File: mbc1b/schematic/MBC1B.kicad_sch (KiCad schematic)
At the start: 25 parts, among them U1 ODRV, U10 ODRV, U2 ODRV, U3 ODRV, U4 ODRV, U5 ODRV, U6 ODRV, U7 ODRV, U8 ODRV, U9 ODRV

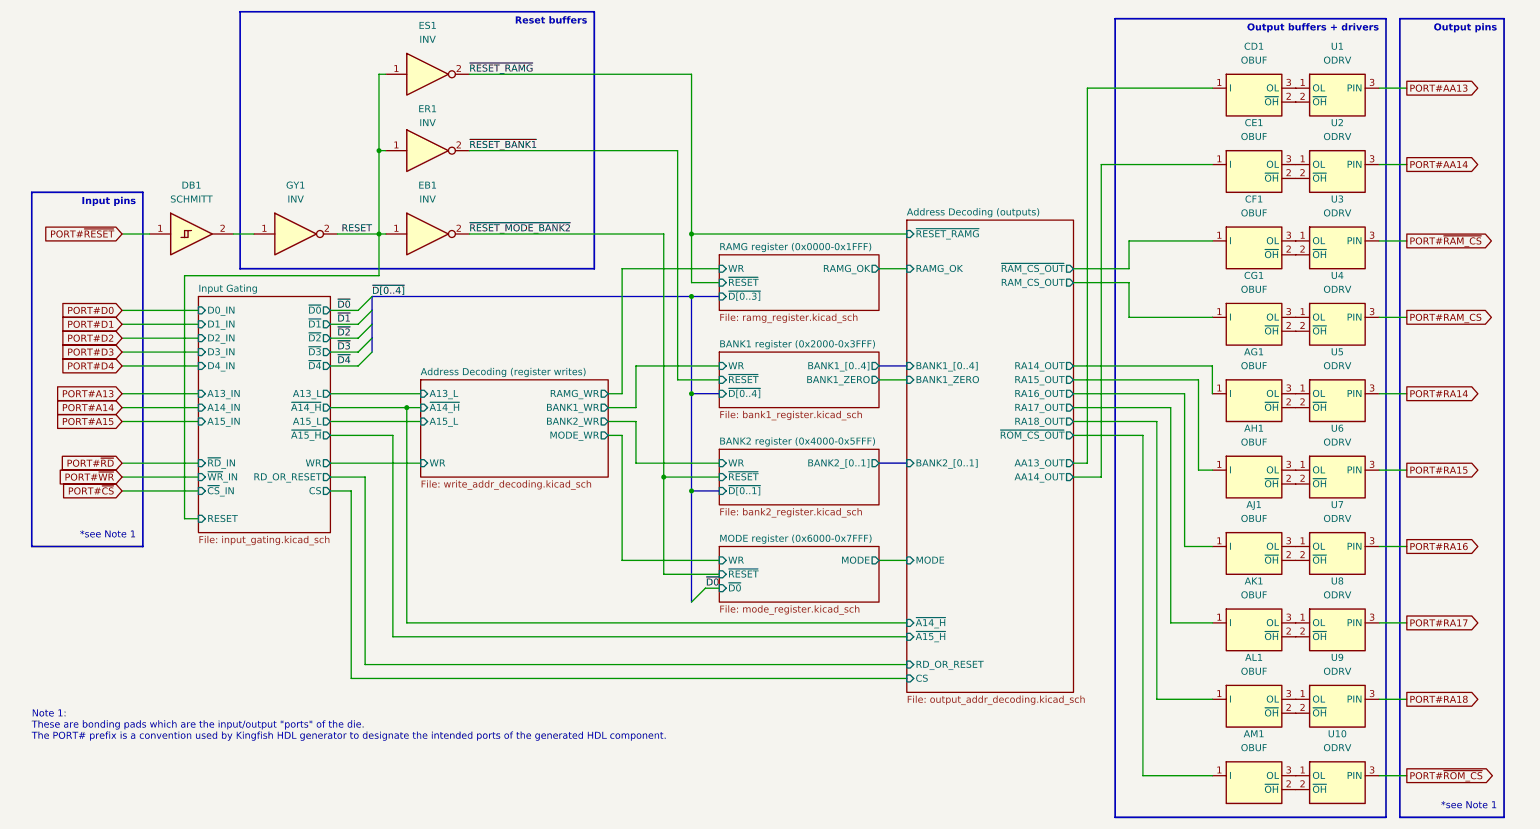
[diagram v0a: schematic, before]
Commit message: Update MBC1B schematic with latest kingfish compatibility
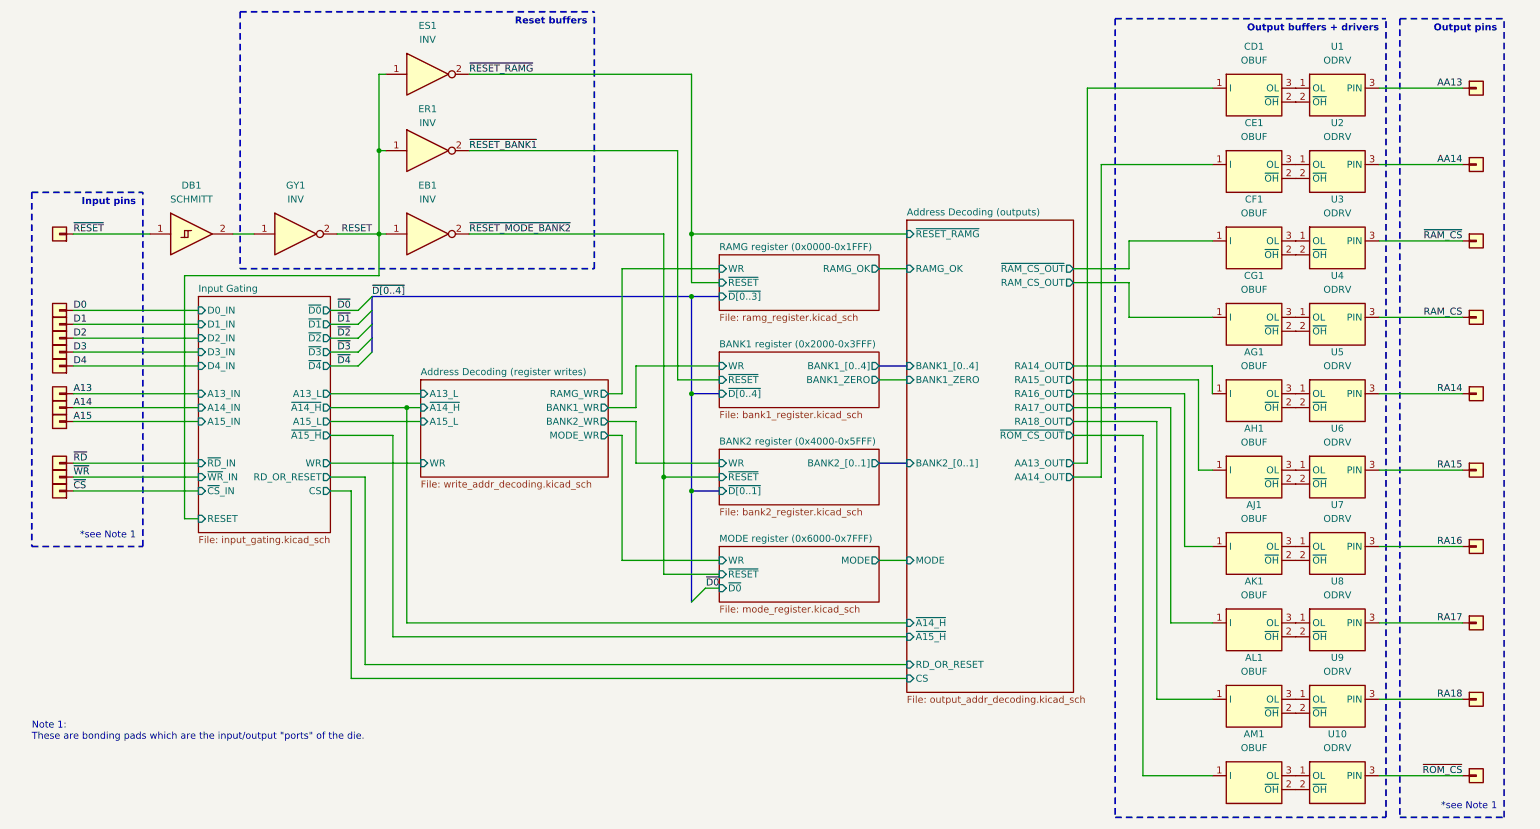
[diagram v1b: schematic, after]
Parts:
- added A1, A10, A11, A12, A2, A3, A4, A5, A6, A7, A8, A9: ~, symbol Kingfish:Kingfish_Port_In
- added A13, A14, A15, A16, A17, A18, A19, A20, A21, A22: ~, symbol Kingfish:Kingfish_Port_Out
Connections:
- net PORT#AA13 renamed AA13
- net AA13: now also A13.1 (kingfish:port)
- net PORT#AA14 renamed AA14
- net AA14: now also A14.1 (kingfish:port)
- net PORT#RA14 renamed RA14
- net RA14: now also A17.1 (kingfish:port)
- net PORT#RA15 renamed RA15
- net RA15: now also A18.1 (kingfish:port)
- net PORT#RA16 renamed RA16
- net RA16: now also A19.1 (kingfish:port)
- net PORT#RA17 renamed RA17
- net RA17: now also A20.1 (kingfish:port)
- net PORT#RA18 renamed RA18
- net RA18: now also A21.1 (kingfish:port)
- net PORT#RAM_CS renamed RAM_CS
- net RAM_CS: now also A16.1 (kingfish:port)
- net PORT#~{RAM_CS} renamed ~{RAM_CS}
- net ~{RAM_CS}: now also A15.1 (kingfish:port)
- net PORT#~{RESET} renamed ~{RESET}
- net ~{RESET}: now also A1.1 (kingfish:port)
- net PORT#~{ROM_CS} renamed ~{ROM_CS}
- net ~{ROM_CS}: now also A22.1 (kingfish:port)
- new net A13: A7.1 (kingfish:port)
- new net A14: A8.1 (kingfish:port)
- new net A15: A9.1 (kingfish:port)
- new net D0: A2.1 (kingfish:port)
- new net D1: A3.1 (kingfish:port)
- new net D2: A4.1 (kingfish:port)
- new net D3: A5.1 (kingfish:port)
- new net D4: A6.1 (kingfish:port)
- new net ~{CS}: A12.1 (kingfish:port)
- new net ~{RD}: A10.1 (kingfish:port)
- new net ~{WR}: A11.1 (kingfish:port)
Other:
- note added: "Note 1: These are bonding pads which are the input/output "ports" of the die."
- note removed: "Note 1: These are bonding pads which are the input/output "ports" of the die. The PORT# prefix is a convention used by Kingfish HDL generator to designate the intended ports of the generated HDL component."
